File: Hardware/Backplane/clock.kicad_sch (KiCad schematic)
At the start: 10 parts, among them U201 OSC48M-3.3I/S3-20T, U202 NL17SZS11DFT2G-Q, U203 NL17SZS11DFT2G-Q, U204 NL17SZS11DFT2G-Q, U205 NL17SZS11DFT2G-Q

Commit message: Updates the backplane to fit the new platform definition, replaces now deprecated RTC with a new one, improves power management.
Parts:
- R201: now in the parts list
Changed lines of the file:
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@@
 		(body_style 1)
 		(exclude_from_sim no)
-		(in_bom no)
+		(in_bom yes)
 		(on_board yes)
 		(in_pos_files yes)

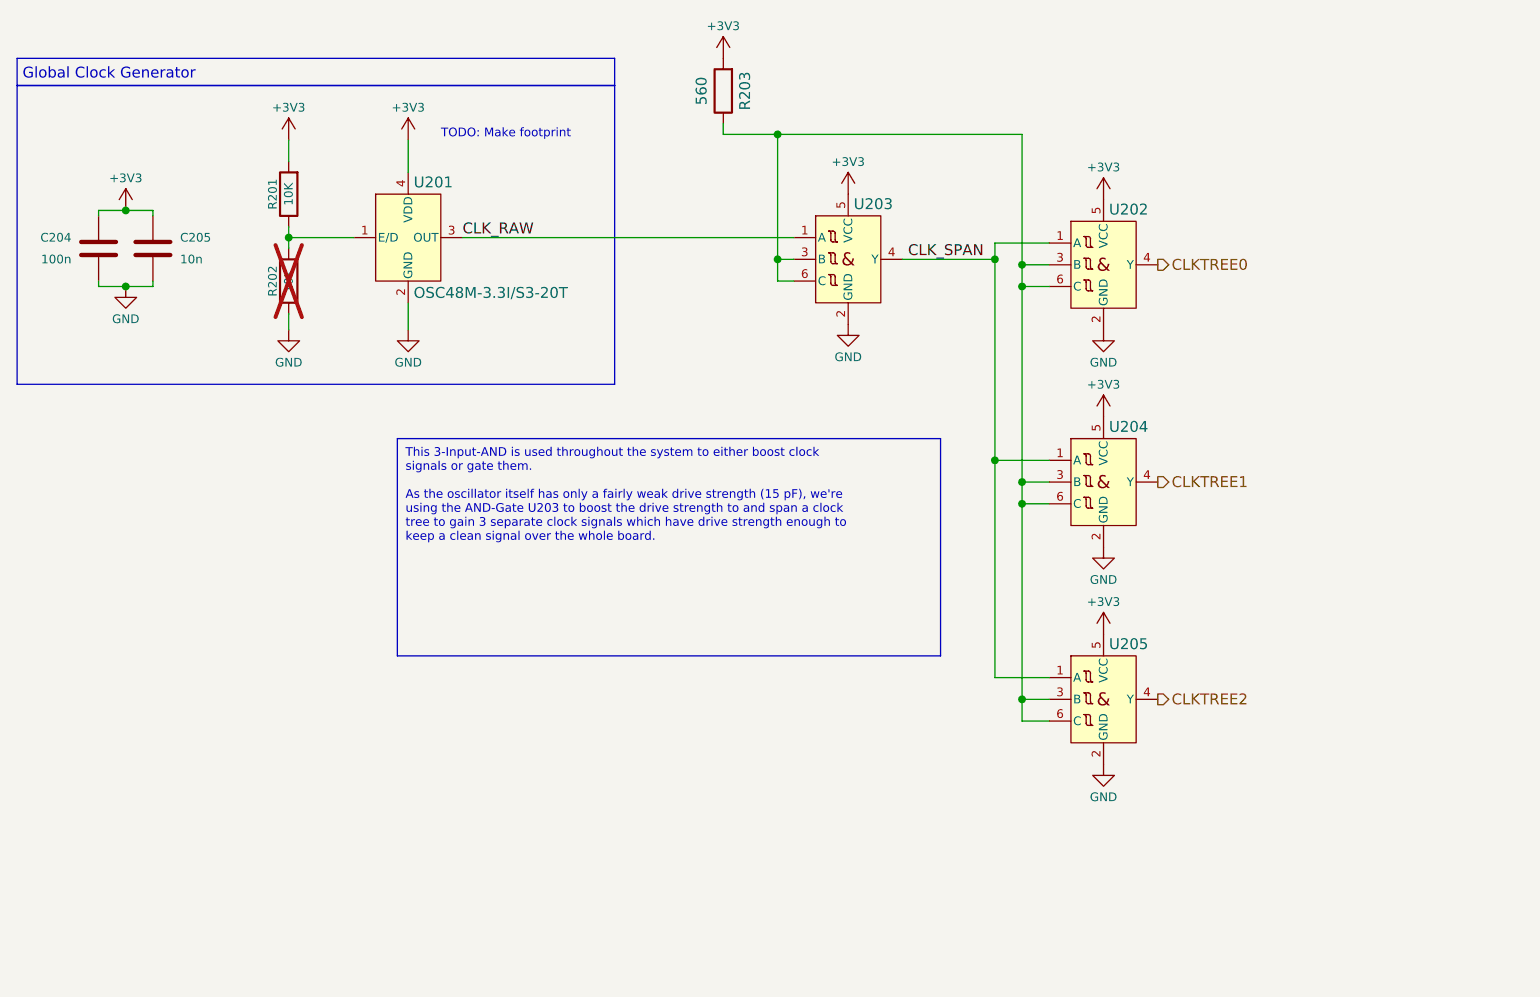
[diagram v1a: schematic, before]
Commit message: Improves backplane schematic even more
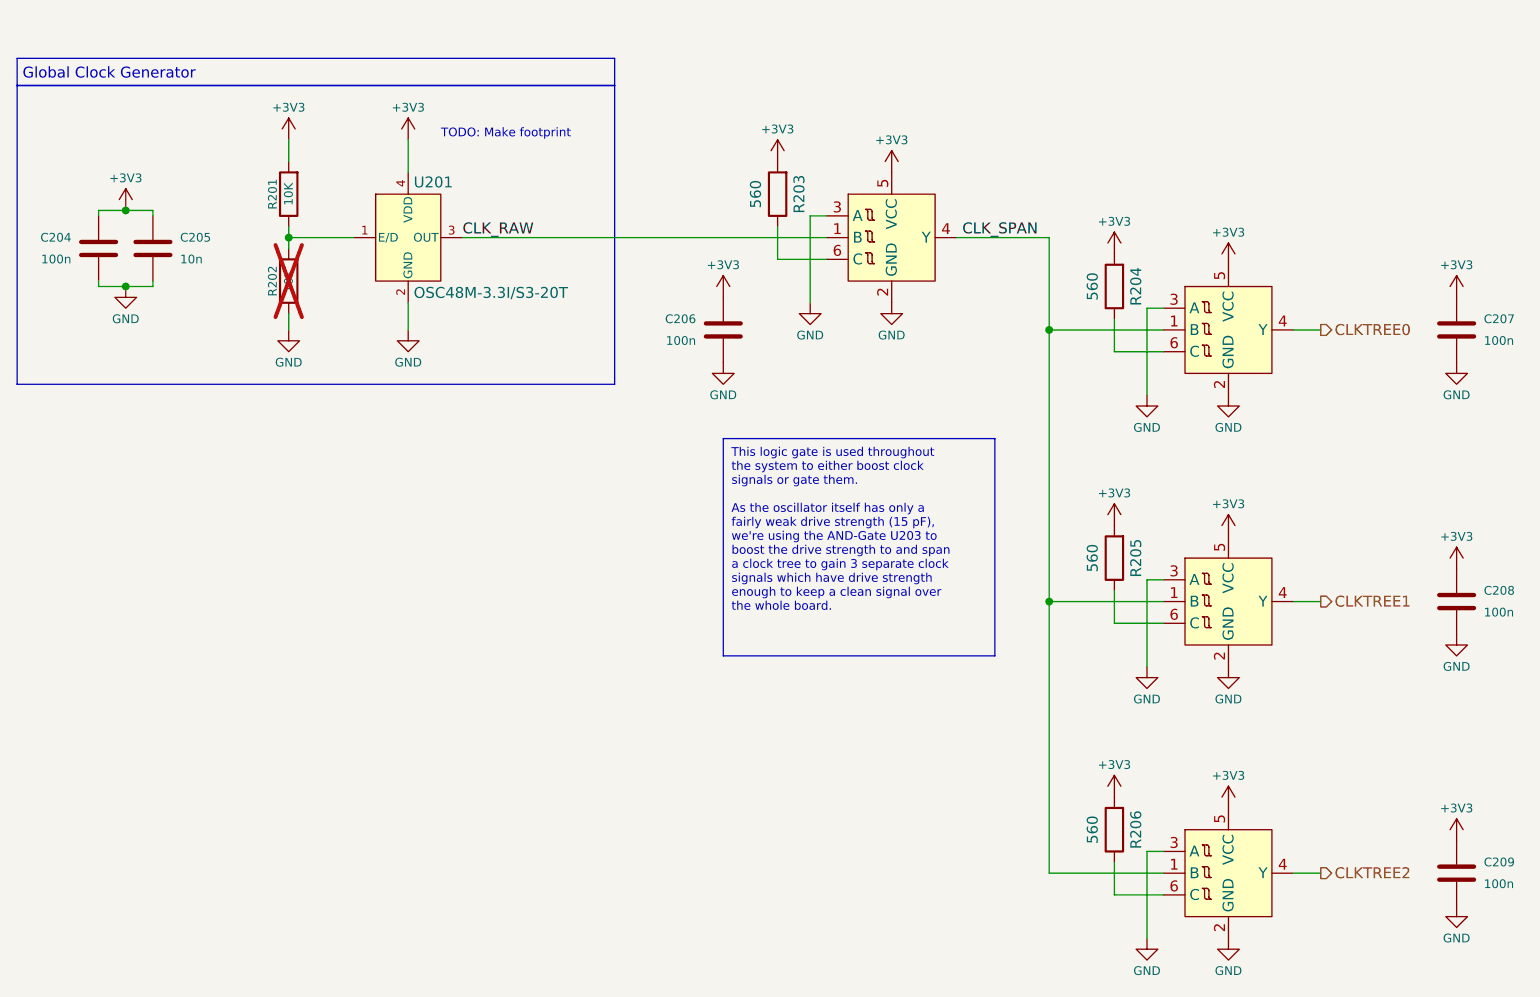
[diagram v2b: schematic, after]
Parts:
- removed U202, U203, U204, U205: NL17SZS11DFT2G-Q, Package_TO_SOT_SMD:SOT-363_SC-70-6, symbol Home Computer:NL17SZS11DFT2G-Q
- added C206, C207, C208, C209: 100n, Capacitor_SMD:C_0603_1608Metric, symbol Device:C
- added R204, R205, R206: 560, Resistor_SMD:R_0603_1608Metric, symbol Device:R
- added U26, U27, U28, U29: NL7SZ57DBVT1G, Package_TO_SOT_SMD:SC-74-6_1.55x2.9mm_P0.95mm, symbol Home Computer:NL7SZ57DBVT1G
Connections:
- net +3V3: now also C206.2, C207.2, C208.2, C209.2, R204.2, R205.2, R206.2, U26.5 (VCC), U27.5 (VCC), U28.5 (VCC), U29.5 (VCC)
- net CLKTREE0: now also U27.4 (Y)
- net CLKTREE1: now also U28.4 (Y)
- net CLKTREE2: now also U29.4 (Y)
- net CLK_RAW: now also U26.1 (B)
- net CLK_SPAN: now also U26.4 (Y), U27.1 (B), U28.1 (B), U29.1 (B)
- net GND: now also C206.1, C207.1, C208.1, C209.1, U26.2 (GND), U26.3 (A), U27.2 (GND), U27.3 (A), U28.2 (GND), U28.3 (A), U29.2 (GND), U29.3 (A)
- net at R203.1: now also U26.6 (C)
- new net: R205.1, U28.6 (C)
- new net: R206.1, U29.6 (C)
- new net: R204.1, U27.6 (C)
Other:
- moved on the sheet: R203
